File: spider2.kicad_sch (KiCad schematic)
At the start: 67 parts, among them J1 NRJ6HH, J10 20-1655, J11 20-1655, J12 20-1655, J13 20-1655, J14 20-1655, J15 20-1655, J16 20-1655, J17 3.5mm Jack, J18 3.5mm Jack, J2 NRJ6HH, J3 20-1655, J4 20-1655, J5 20-1655, J6 20-1655, J7 20-1655, J8 20-1655, J9 20-1655, P1 USB4085, Q1 BC547, Q2 BC547, Q3 AOI21357, SW2 EG2315, U1 LM386N-1, U2 LM386N-1, U3 LM4562, U4 LM7805_TO220

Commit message: re-annotate schematic
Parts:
- renumbered C6 to C2, C2 to C4, C4 to C5, C7 to C6, C5 to C7, D4 to D1, D1 to D2, D2 to D3, D3 to D4, J7 to J10, J4 to J3, J5 to J4, J6 to J5, J3 to J6, J8 to J7, J9 to J8, J10 to J9, Q3 to Q1, Q1 to Q2, Q2 to Q3, R6 to R10, R10 to R11, R11 to R12, R12 to R13, R15 to R14, R16 to R15, R17 to R16, R13 to R17, R14 to R18, R22 to R19, R27 to R2, R23 to R20, R18 to R21, R19 to R22, R20 to R23, R21 to R24, R24 to R25, R25 to R26, R26 to R27, R2 to R6, SW2 to SW1, U4 to U2, U2 to U3, U3 to U4

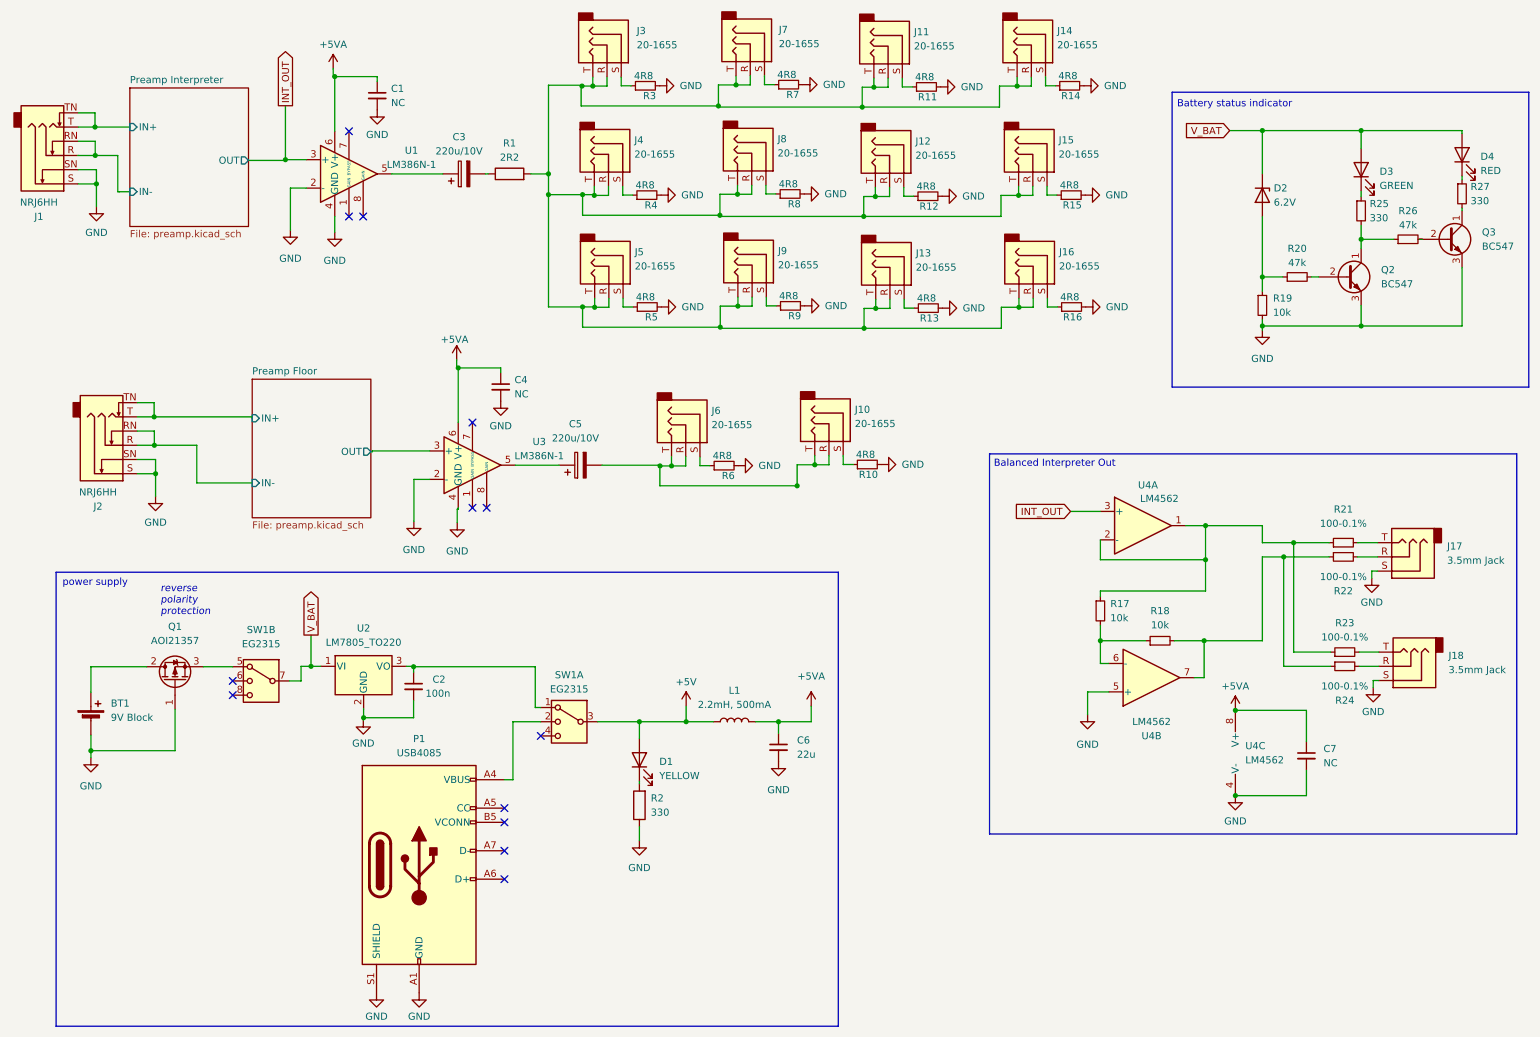
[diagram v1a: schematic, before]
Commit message: incorporate review feedback on schematic + pcb design
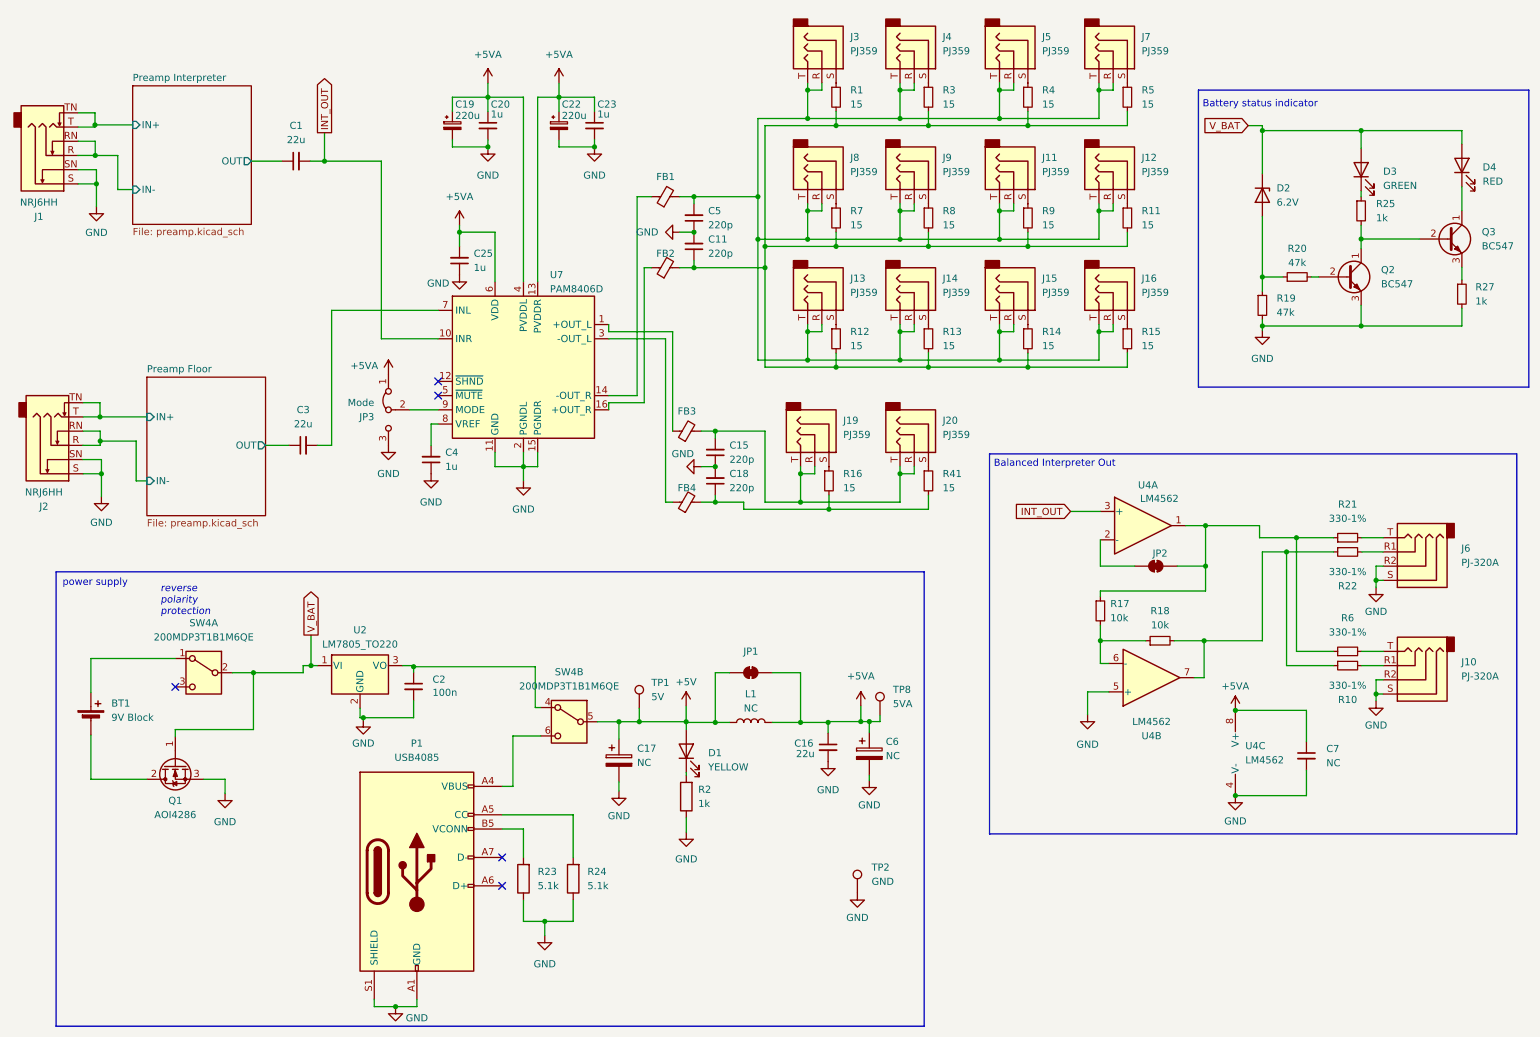
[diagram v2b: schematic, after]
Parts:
- removed C3, C5: 220u/10V, Capacitor_THT:CP_Radial_D6.3mm_P2.50mm, symbol Device:C_Polarized
- removed C6: 22u, symbol Device:C_Small
- removed J10, J6: 20-1655, symbol Connector_Audio:AudioJack3
- removed J17, J18: 3.5mm Jack, symbol Connector_Audio:AudioJack3
- removed Q1: AOI21357, symbol Device:Q_PMOS_GDS
- removed R1: 2R2, symbol Device:R
- removed R23, R24: 100-0.1%, symbol Device:R_Small
- removed R26: 47k, symbol Device:R_Small
- removed SW1: EG2315, symbol Switch:SW_DP3T
- removed U1, U3: LM386N-1, Package_DIP:DIP-8_W7.62mm_Socket, symbol Amplifier_Audio:LM386
- added C11, C15, C18, C5: 220p, Capacitor_THT:C_Disc_D5.1mm_W3.2mm_P5.00mm, symbol Device:C_Small
- added C16, C3: 22u, Capacitor_THT:C_Disc_D5.1mm_W3.2mm_P5.00mm, symbol Device:C_Small
- added C17, C6: NC, Capacitor_THT:CP_Radial_D6.3mm_P2.50mm, symbol Device:C_Polarized
- added C19, C22: 220u, Capacitor_THT:CP_Radial_D6.3mm_P2.50mm, symbol Device:C_Polarized_Small
- added C20, C23, C25: 1u, Capacitor_THT:C_Disc_D5.1mm_W3.2mm_P5.00mm, symbol Device:C_Small
- added FB1, FB2, FB3, FB4: FerriteBead_Small, Inductor_THT:L_Axial_L7.0mm_D3.3mm_P10.16mm_Horizontal_Fastron_MICC, symbol Device:FerriteBead_Small
- added J10, J6: PJ-320A, custom:Jack_3.5mm_PJ320A, symbol Connector_Audio:AudioJack4
- added J19, J20: PJ359, custom:Jack_3.5mm_PJ359, symbol Connector_Audio:AudioJack3
- added JP1, JP2: SolderJumper_2_Bridged, Jumper:SolderJumper-2_P1.3mm_Bridged_RoundedPad1.0x1.5mm, symbol Jumper:SolderJumper_2_Bridged
- added JP3: Mode, Jumper:SolderJumper-3_P1.3mm_Bridged12_RoundedPad1.0x1.5mm, symbol Jumper:Jumper_3_Bridged12
- added Q1: AOI4286, Package_TO_SOT_THT:TO-251-3_Vertical, symbol Device:Q_NMOS_GDS
- added R1, R41: 15, Resistor_THT:R_Axial_DIN0207_L6.3mm_D2.5mm_P10.16mm_Horizontal, symbol Device:R_Small
- added R23, R24: 5.1k, Resistor_THT:R_Axial_DIN0207_L6.3mm_D2.5mm_P10.16mm_Horizontal, symbol Device:R
- added SW4: 200MDP3T1B1M6QE, Button_Switch_THT:SW_Push_2P2T_Vertical_E-Switch_800UDP8P1A1M6, symbol Switch:SW_DPDT_x2
- added TP1: 5V, TestPoint:TestPoint_THTPad_1.5x1.5mm_Drill0.7mm, symbol Connector:TestPoint
- added TP2: GND, TestPoint:TestPoint_THTPad_1.5x1.5mm_Drill0.7mm, symbol Connector:TestPoint
- added TP8: 5VA, TestPoint:TestPoint_THTPad_1.5x1.5mm_Drill0.7mm, symbol Connector:TestPoint
- added U7: PAM8406D, Package_SO:SOP-16_3.9x9.9mm_P1.27mm, symbol Amplifier_Audio:PAM8406D
- BT1: footprint (none) -> Connector_PinHeader_2.54mm:PinHeader_1x02_P2.54mm_Vertical
- C1: value NC -> 22u; footprint (none) -> Capacitor_THT:C_Disc_D5.1mm_W3.2mm_P5.00mm
- C2, C7: footprint (none) -> Capacitor_THT:C_Disc_D5.1mm_W3.2mm_P5.00mm
- C4: value NC -> 1u; footprint (none) -> Capacitor_THT:C_Disc_D5.1mm_W3.2mm_P5.00mm
- D1: footprint (none) -> LED_THT:LED_D5.0mm_FlatTop
- D2: footprint (none) -> Diode_THT:D_DO-35_SOD27_P7.62mm_Horizontal
- D3, D4: footprint (none) -> LED_THT:LED_D3.0mm_FlatTop
- J11, J12, J13, J14, J15, J16, J4, J5, J8, J9: value 20-1655 -> PJ359; footprint (none) -> custom:Jack_3.5mm_PJ359
- J3, J7: value 20-1655 -> PJ359; footprint Connector_Audio:Jack_3.5mm_QingPu_WQP-PJ398SM_Vertical_CircularHoles -> custom:Jack_3.5mm_PJ359
- L1: value 2.2mH, 500mA -> NC; footprint (none) -> Inductor_THT:L_Radial_D8.7mm_P5.00mm_Fastron_07HCP
- R10, R6: value 4R8 -> 330-1%; footprint (none) -> Resistor_THT:R_Axial_DIN0207_L6.3mm_D2.5mm_P10.16mm_Horizontal
- R11, R12, R13, R14, R15, R16, R3, R4, R5, R7, R8, R9: value 4R8 -> 15; footprint (none) -> Resistor_THT:R_Axial_DIN0207_L6.3mm_D2.5mm_P10.16mm_Horizontal
- R17, R18, R20: footprint (none) -> Resistor_THT:R_Axial_DIN0207_L6.3mm_D2.5mm_P10.16mm_Horizontal
- R19: value 10k -> 47k; footprint (none) -> Resistor_THT:R_Axial_DIN0207_L6.3mm_D2.5mm_P10.16mm_Horizontal
- R2, R25, R27: value 330 -> 1k; footprint (none) -> Resistor_THT:R_Axial_DIN0207_L6.3mm_D2.5mm_P10.16mm_Horizontal
- R21, R22: value 100-0.1% -> 330-1%; footprint (none) -> Resistor_THT:R_Axial_DIN0207_L6.3mm_D2.5mm_P10.16mm_Horizontal
- U2: footprint Package_TO_SOT_THT:TO-220-3_Vertical -> Package_TO_SOT_THT:TO-220-4_Horizontal_TabDown
- U4: footprint Package_DIP:DIP-8_W7.62mm_Socket -> Package_DIP:DIP-8_W7.62mm
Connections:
- net +5V: now also C17.1, JP1.1 (A), SW4.5 (B), TP1.1
- net +5VA: now also C16.1, C19.1, C20.1, C22.1, C23.1, C25.2, C6.1, JP1.2 (B), JP3.1 (A), TP8.1, U7.13 (PVDDR), U7.4 (PVDDL), U7.6 (VDD); no longer C1.1, C4.1
- net GND: now also C4.1, R27.2, C11.2, C15.1, C16.2, C17.2, C18.2, C19.2, C20.2, C22.2, C23.2, C25.1, C5.1, C6.2, J10.R2, J10.S, J6.R2, J6.S, JP3.3 (B), Q1.3 (S), R23.1, R24.1, TP2.1, U7.11 (GND), U7.15 (PGNDR), U7.2 (PGNDL); no longer BT1.2 (-), C1.2, C4.2, Q3.3 (E), R10.2, R11.2, R12.2, R13.2, R14.2, R15.2, R16.2, R3.2, R4.2, R5.2, R6.2, R7.2, R8.2, R9.2
- net INT_OUT: now also C1.2, U7.10 (INR)
- net Preamp Floor/OUT: now also C3.1
- net V_BAT: now also Q1.1 (G), SW4.2 (B)
- net at BT1.1 (+): now also SW4.1 (A)
- net at J13.S: now also R12.1; no longer R13.1
- net at J11.R, J11.T, J12.R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: now also C5.2, FB1.2
- net at R14.1: now also J15.S; no longer J14.S
- net at R18.2, R22.1, U4.7: now also R10.1
- net at R6.1: now also R17.1, R21.1, U4.1, JP2.2 (B)
- net at R22.2: now also J6.R1
- net at J4.S: now also R3.1; no longer R4.1
- net at J3.S: now also R1.1; no longer R3.1
- net at Q2.1 (C), R25.2: now also Q3.2 (B)
- net at J12.S: now also R11.1; no longer R12.1
- net at D4.1 (K): now also Q3.1 (C); no longer R27.1
- net at J11.S: now also R9.1; no longer R11.1
- net at J7.S: now also R5.1; no longer R7.1
- net at J9.S: now also R8.1; no longer R9.1
- net at C2.1, U2.3 (VO): now also SW4.4 (A)
- net at J5.S: now also R4.1; no longer R5.1
- net at J8.S: now also R7.1; no longer R8.1
- net at R21.2: now also J6.T
- net at R15.1: now also J16.S; no longer J15.S
- net at R16.1: now also J19.S; no longer J16.S
- net at P1.A4 (VBUS), P1.A9 (VBUS), P1.B4 (VBUS)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: now also SW4.6 (C)
- net at P1.A5 (CC): now also R24.2
- net at P1.B5 (VCONN): now also R23.2
- new net: J10.T, R6.2
- new net: C18.1, FB4.2, R16.2, R41.2
- new net: C11.1, FB2.2, R1.2, R11.2, R12.2, R13.2, R14.2, R15.2, R3.2, R4.2, R5.2, R7.2, R8.2, R9.2
- new net: J10.R1, R10.2
- new net: J20.S, R41.1
- new net: J14.S, R13.1
- new net: FB3.1, U7.1 (+OUT_L)
- new net: FB1.1, U7.14 (-OUT_R)
- new net: FB2.1, U7.16 (+OUT_R)
- new net: FB4.1, U7.3 (-OUT_L)
- new net: C3.2, U7.7 (INL)
- new net: C4.2, U7.8 (VREF)
- new net: JP3.2 (C), U7.9 (MODE)
- new net: C15.2, FB3.2, J19.R, J19.T, J20.R, J20.T
- new net: BT1.2 (-), Q1.2 (D)
- new net: Q3.3 (E), R27.1
- new net: JP2.1 (A), U4.2 (-)
- new net Preamp Interpreter/OUT: C1.1
- no-connect marks 13 -> 5
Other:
- moved on the sheet: D1, D4, J2, L1, P1, R2, R21, R22, R27, U2

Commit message: 3.3V step down, fixed wrong CMV on balanced out, additional SMD footprints
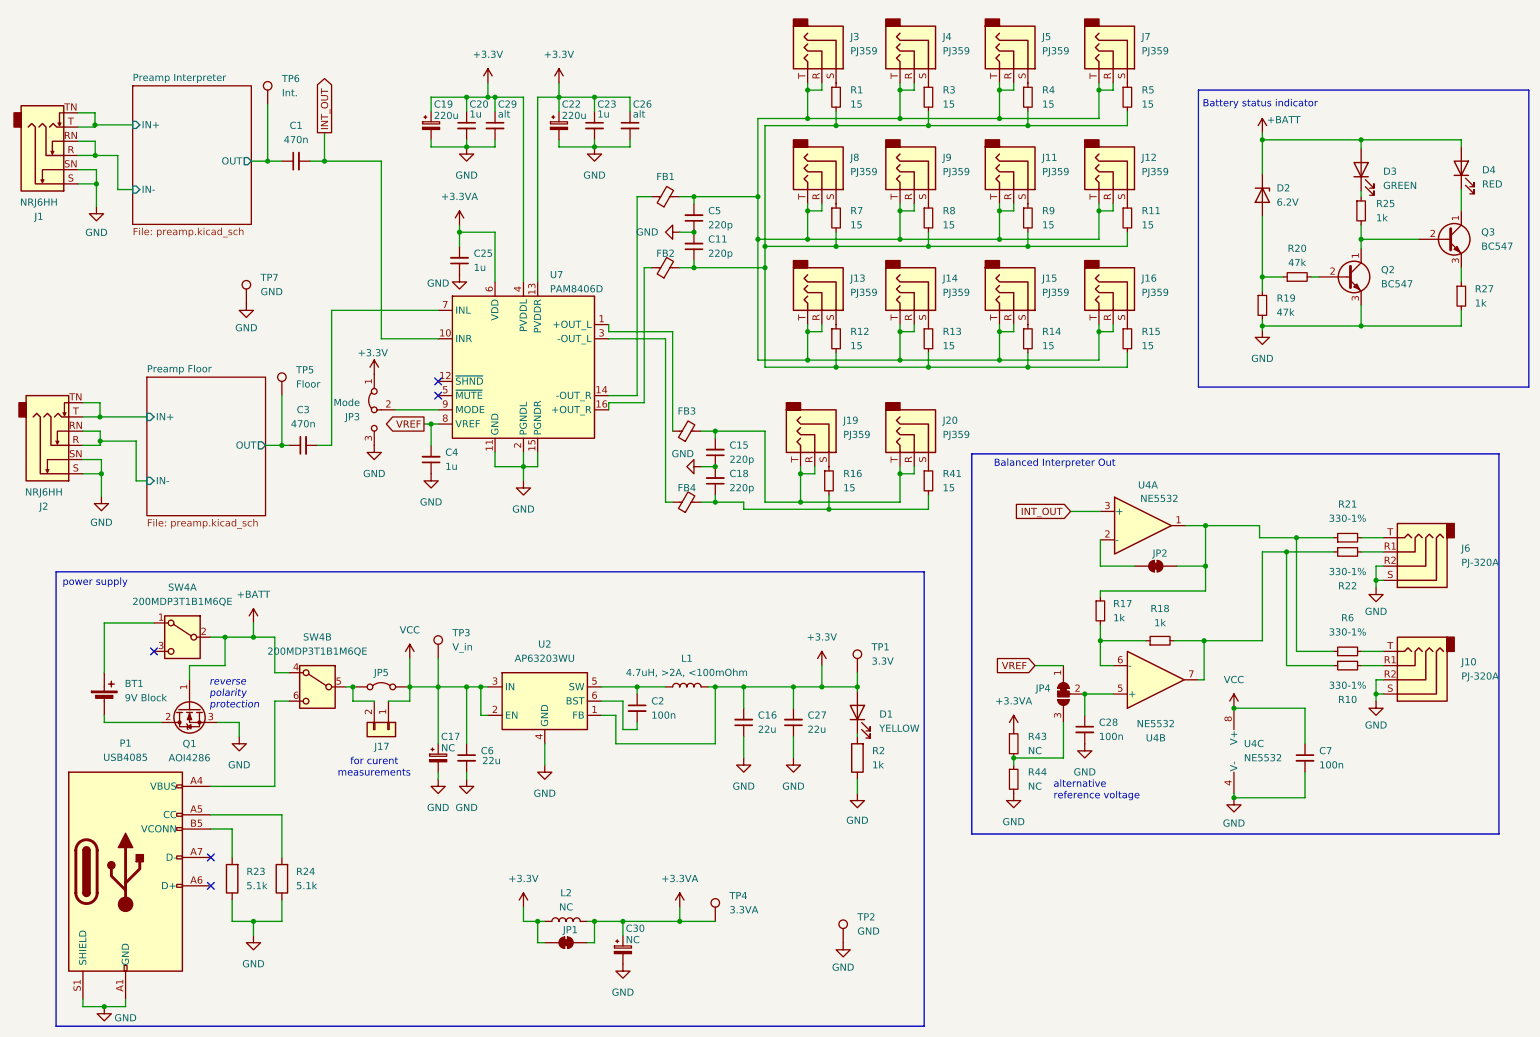
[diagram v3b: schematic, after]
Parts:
- removed C17, C6: NC, Capacitor_THT:CP_Radial_D6.3mm_P2.50mm, symbol Device:C_Polarized
- removed TP8: 5VA, TestPoint:TestPoint_THTPad_1.5x1.5mm_Drill0.7mm, symbol Connector:TestPoint
- removed U2: LM7805_TO220, Package_TO_SOT_THT:TO-220-4_Horizontal_TabDown, symbol Regulator_Linear:LM7805_TO220
- added C17, C30: NC, Capacitor_THT:CP_Radial_D6.3mm_P2.50mm, symbol Device:C_Polarized_Small
- added C26, C29: alt, Capacitor_SMD:C_0805_2012Metric_Pad1.18x1.45mm_HandSolder, symbol Device:C_Small
- added C27, C6: 22u, Capacitor_THT:C_Disc_D5.1mm_W3.2mm_P5.00mm, symbol Device:C_Small
- added C28: 100n, Capacitor_THT:C_Disc_D5.1mm_W3.2mm_P5.00mm, symbol Device:C_Small
- added J17: A, Connector_PinHeader_2.54mm:PinHeader_1x02_P2.54mm_Vertical, symbol Connector_Generic:Conn_01x02
- added JP4: SolderJumper_3_Bridged12, Jumper:SolderJumper-3_P1.3mm_Bridged12_RoundedPad1.0x1.5mm, symbol Jumper:SolderJumper_3_Bridged12
- added JP5: Jumper_2_Bridged, Jumper:SolderJumper-2_P1.3mm_Bridged_RoundedPad1.0x1.5mm, symbol Jumper:Jumper_2_Bridged
- added L2: NC, Inductor_THT:L_Axial_L5.3mm_D2.2mm_P10.16mm_Horizontal_Vishay_IM-1, symbol Device:L
- added R43, R44: NC, Resistor_THT:R_Axial_DIN0207_L6.3mm_D2.5mm_P10.16mm_Horizontal, symbol Device:R_Small
- added TP3: V_in, TestPoint:TestPoint_THTPad_1.5x1.5mm_Drill0.7mm, symbol Connector:TestPoint
- added TP4: 3.3VA, TestPoint:TestPoint_THTPad_1.5x1.5mm_Drill0.7mm, symbol Connector:TestPoint
- added TP5: Floor, TestPoint:TestPoint_THTPad_1.5x1.5mm_Drill0.7mm, symbol Connector:TestPoint
- added TP6: Int., TestPoint:TestPoint_THTPad_1.5x1.5mm_Drill0.7mm, symbol Connector:TestPoint
- added TP7: GND, TestPoint:TestPoint_THTPad_4.0x4.0mm_Drill2.0mm, symbol Connector:TestPoint
- added U2: AP63203WU, Package_TO_SOT_SMD:TSOT-23-6, symbol Regulator_Switching:AP63203WU
- C1, C3: value 22u -> 470n
- C7: value NC -> 100n
- L1: value NC -> 4.7uH, >2A, <100mOhm
- R17, R18: value 10k -> 1k
- TP1: value 5V -> 3.3V
- TP2: footprint TestPoint:TestPoint_THTPad_1.5x1.5mm_Drill0.7mm -> TestPoint:TestPoint_THTPad_2.5x2.5mm_Drill1.2mm
- U4: value LM4562 -> NE5532
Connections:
- net GND: now also C16.1, C17.2, C26.2, C27.1, C28.2, C29.2, C30.2, C6.2, R44.2, TP7.1, U2.4 (GND); no longer C16.2, C2.2, U4.5 (+)
- net Preamp Floor/OUT: now also TP5.1
- net Preamp Interpreter/OUT: now also TP6.1
- net VREF: now reaches C4.2, U7.8 (VREF)
- net VREF: now also JP4.1 (A)
- net at C2.1: now also L1.1, U2.5 (SW); no longer SW4.4 (A)
- net +5V renamed +3.3V
- net +3.3V: now also C16.2, C19.1, C20.1, C22.1, C23.1, JP3.1 (A), L1.2, U7.13 (PVDDR), U7.4 (PVDDL), C26.1, C27.2, C29.1, L2.1, U2.1 (FB); no longer L1.1, SW4.5 (B)
- removed net +5VA: C16.1, C19.1, C20.1, C22.1, C23.1, C25.2, C7.1, JP1.2 (B), JP3.1 (A), L1.2, U4.8 (V+), U7.13 (PVDDR), U7.4 (PVDDL), U7.6 (VDD)
- net V_BAT renamed +BATT
- net +BATT: now also SW4.4 (A)
- new net: C28.1, JP4.2 (C), U4.5 (+)
- new net: JP4.3 (B), R43.2, R44.1
- new net: C2.2, U2.6 (BST)
- new net: J17.2 (Pin_2), JP5.1 (A), SW4.5 (B)
- new net +3.3VA: C25.2, C30.1, JP1.2 (B), L2.2, R43.1, TP4.1, U7.6 (VDD)
- new net VCC: C17.1, C6.1, C7.1, J17.1 (Pin_1), JP5.2 (B), TP3.1, U2.2 (EN), U2.3 (IN), U4.8 (V+)
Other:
- note added: "alternative reference voltage"
- note added: "for curent measurements"
- title: (none) -> Spider2
- moved on the sheet: BT1, C19, C20, D1, D4, JP3, P1, Q1, R2, R23, R24, TP2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

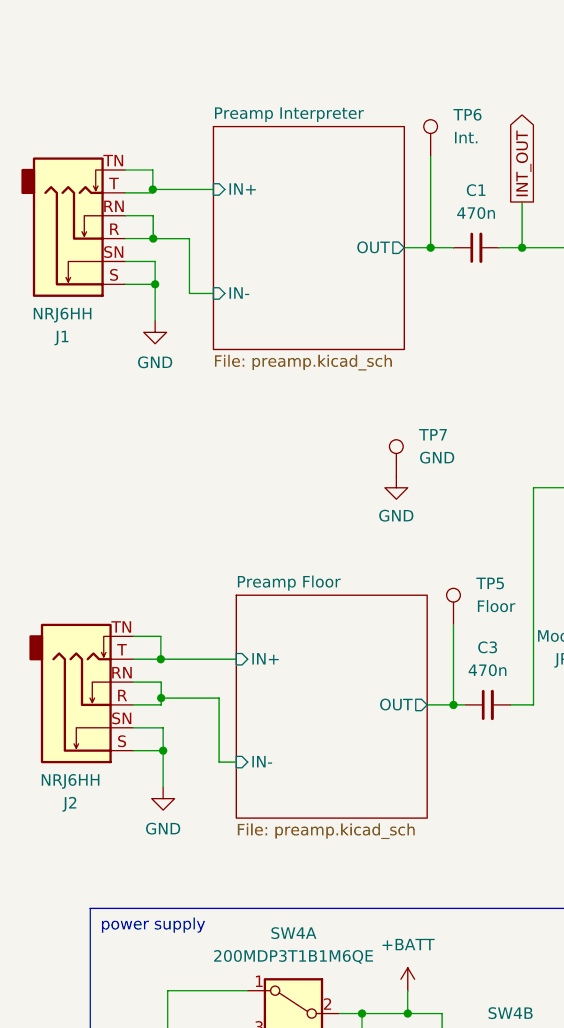
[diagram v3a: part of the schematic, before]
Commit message: jumper for switching input jacks between GND and BIAS
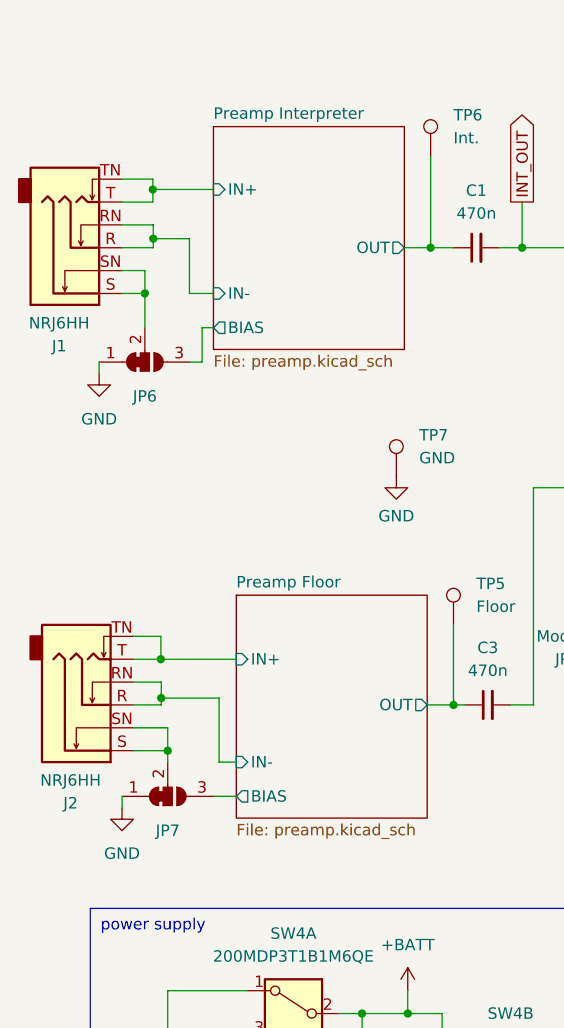
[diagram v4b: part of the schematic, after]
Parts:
- added JP6, JP7: SolderJumper_3_Bridged12, Jumper:SolderJumper-3_P1.3mm_Bridged12_RoundedPad1.0x1.5mm, symbol Jumper:SolderJumper_3_Bridged12
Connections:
- net GND: now also JP6.1 (A), JP7.1 (A); no longer J1.S, J1.SN, J2.S, J2.SN
- new net: J1.S, J1.SN, JP6.2 (C)
- new net: J2.S, J2.SN, JP7.2 (C)
- new net Preamp Floor/BIAS: JP7.3 (B)
- new net Preamp Interpreter/BIAS: JP6.3 (B)
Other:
- sheet Preamp Floor ports: added BIAS; removed none
- sheet Preamp Interpreter ports: added BIAS; removed none
- moved on the sheet: J1
